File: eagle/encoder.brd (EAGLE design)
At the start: 100 x 80 mm, 11 parts, among them IC1 LM339D, U1 MCP42XXX

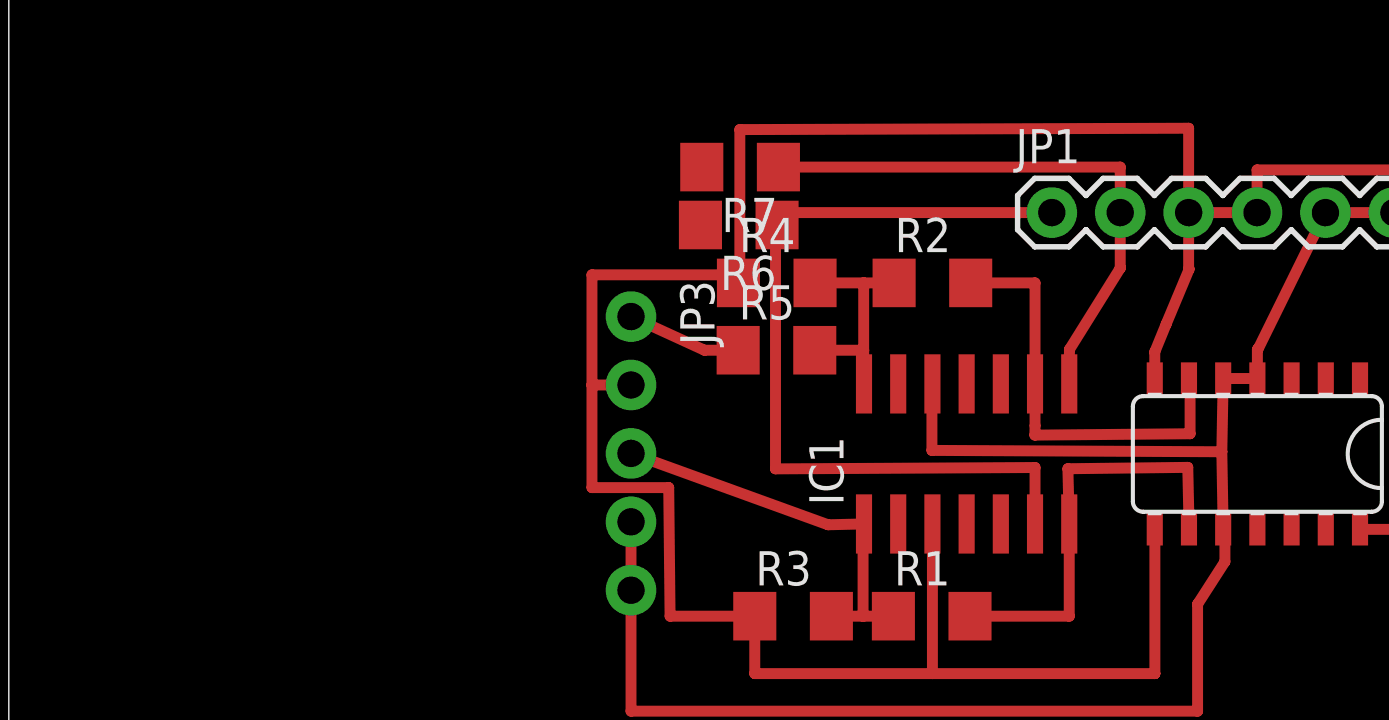
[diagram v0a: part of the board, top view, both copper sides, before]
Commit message: Added atmega.
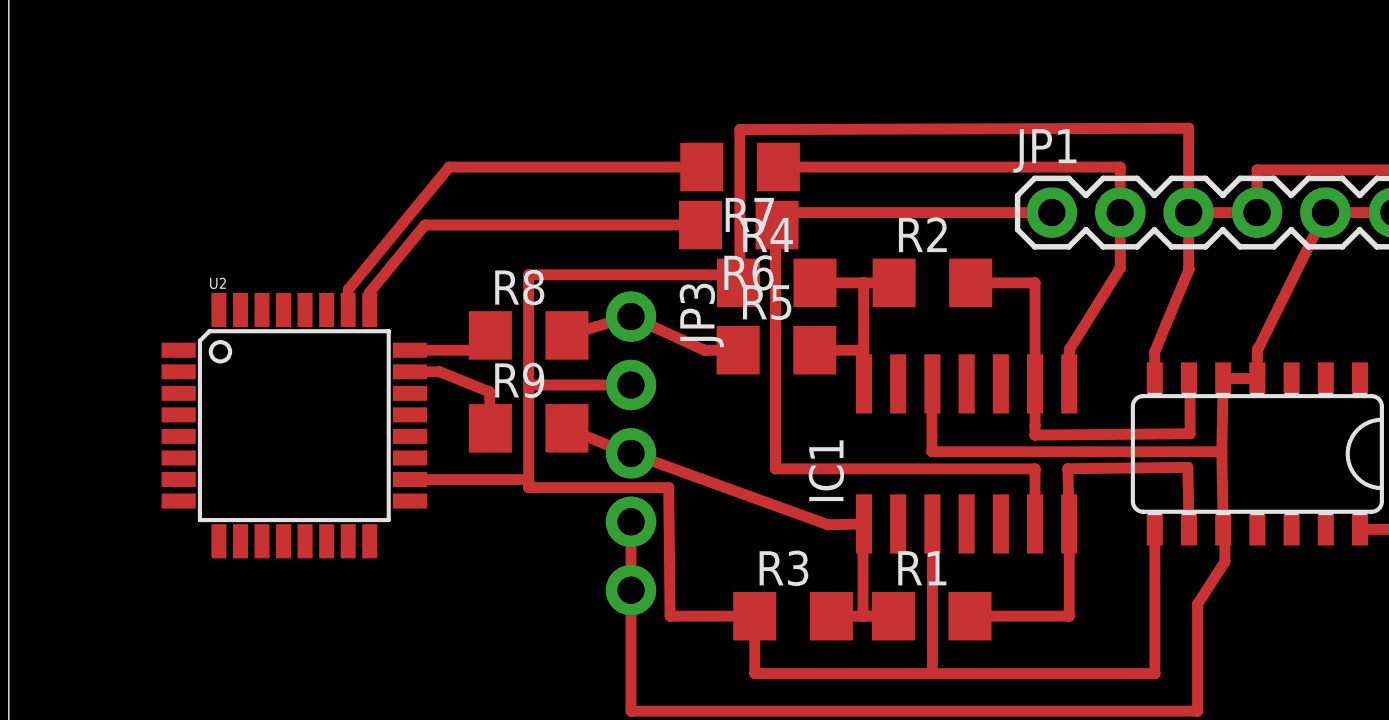
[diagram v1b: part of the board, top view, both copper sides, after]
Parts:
- added R8, R9: 0, resistor:R1206
- added U2: ATMEGA328P, SparkFun-DigitalIC:TQFP32-08
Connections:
- removed net N$2: IC1.1, JP3.3, R1.1, R3.2
- removed net N$4: JP3.1, R5.1
- new net A-ANALOG-IN: R7.2, U2.26
- new net A-DIGITAL-IN: IC1.1, JP3.3, R1.1, R3.2, R9.2
- new net B-ANALOG-IN: R6.2, U2.25
- new net B-DIGITAL-IN: JP3.1, R5.1, R8.2
- new net N$6: R8.1, U2.24
- new net N$7: R9.1, U2.23
- net +5V: now also U2.18
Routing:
- net A-DIGITAL-IN: track 0.00 -> 17.9 mm
- net A-ANALOG-IN: track 0.00 -> 16.0 mm
- net N$2: track 15.2 -> 0.00 mm
- net B-ANALOG-IN: track 0.00 -> 14.1 mm
- net +5V: track 113.3 -> 124.8 mm
- net B-DIGITAL-IN: track 0.00 -> 6.73 mm
- net N$7: track 0.00 -> 4.45 mm
- net N$4: track 4.25 -> 0.00 mm
- net N$6: track 0.00 -> 3.54 mm
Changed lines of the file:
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@@
 <element name="R6" library="resistor" package="R1206" value="0" x="27.1" y="59.3" rot="R180"/>
 <element name="R7" library="resistor" package="R1206" value="0" x="27.15" y="61.45" rot="R180"/>
+<element name="U2" library="SparkFun-DigitalIC" package="TQFP32-08" value="ATMEGA328P" x="10.6" y="51.85">
+<attribute name="PROD_ID" value="IC-09069" x="10.6" y="51.85" size="1.778" layer="27" display="off"/>
+</element>
+<element name="R8" library="resistor" package="R1206" value="0" x="19.3" y="55.2"/>
+<element name="R9" library="resistor" package="R1206" value="0" x="19.3" y="51.75"/>
 </elements>
 <signals>
@@
 <contactref element="JP1" pad="6"/>
 <wire x1="34.29" y1="53.4" x2="34.271946875" y2="53.4" width="0.4064" layer="1"/>
-<wire x1="34.271946875" y1="53.4" x2="34.271946875" y2="50.930871875" width="0.4064" layer="1"/>
-<wire x1="34.271946875" y1="50.930871875" x2="45.035" y2="50.880871875" width="0.4064" layer="1"/>
+<wire x1="34.271946875" y1="53.4" x2="34.271946875" y2="50.880871875" width="0.4064" layer="1"/>
+<wire x1="34.271946875" y1="50.880871875" x2="45.035" y2="50.880871875" width="0.4064" layer="1"/>
 <wire x1="45.035" y1="50.880871875" x2="45.085" y2="53.6" width="0.4064" layer="1"/>
 <wire x1="48.8828875" y1="59.7605125" x2="51.4228875" y2="59.7605125" width="0.4064" layer="1"/>
@@
 <wire x1="23.1" y1="41.25" x2="44.135" y2="41.25" width="0.4064" layer="1"/>
 <wire x1="44.135" y1="41.25" x2="44.135" y2="45.222" width="0.4064" layer="1"/>
-</signal>
-<signal name="N$2">
-<contactref element="R1" pad="1"/>
-<contactref element="R3" pad="2"/>
-<contactref element="IC1" pad="1"/>
-<wire x1="30.53881875" y1="44.776359375" x2="31.715234375" y2="44.776359375" width="0.4064" layer="1"/>
-<wire x1="31.715234375" y1="44.776359375" x2="32.99903125" y2="44.776359375" width="0.4064" layer="1"/>
-<wire x1="32.99903125" y1="44.776359375" x2="32.841440625" y2="44.77635625" width="0.4064" layer="1"/>
-<wire x1="31.75" y1="48.2" x2="31.715234375" y2="48.2" width="0.4064" layer="1"/>
-<contactref element="JP3" pad="3"/>
-<wire x1="31.715234375" y1="48.2" x2="31.715234375" y2="44.776359375" width="0.4064" layer="1"/>
-<wire x1="23.1" y1="50.82" x2="30.415234375" y2="48.17" width="0.4064" layer="1"/>
-<wire x1="30.415234375" y1="48.17" x2="31.715234375" y2="48.2" width="0.4064" layer="1"/>
 </signal>
 <signal name="N$5">
@@
 <wire x1="50.165" y1="48" x2="53.178775" y2="48" width="0.4064" layer="1"/>
 <contactref element="JP3" pad="2"/>
-<wire x1="23.1" y1="53.36" x2="21.65" y2="53.36" width="0.4064" layer="1"/>
-<wire x1="21.65" y1="53.36" x2="21.65" y2="57.45" width="0.4064" layer="1"/>
-<wire x1="21.65" y1="57.45" x2="27.088" y2="57.45" width="0.4064" layer="1"/>
+<wire x1="23.1" y1="53.36" x2="19.3" y2="53.36" width="0.4064" layer="1"/>
+<wire x1="19.3" y1="53.36" x2="19.3" y2="57.45" width="0.4064" layer="1"/>
+<wire x1="19.3" y1="57.45" x2="27.088" y2="57.45" width="0.4064" layer="1"/>
 <wire x1="27.088" y1="57.45" x2="27.088" y2="57.15" width="0.4064" layer="1"/>
 <wire x1="27.69481875" y1="44.776359375" x2="24.55" y2="44.776359375" width="0.4064" layer="1"/>
 <wire x1="24.55" y1="44.776359375" x2="24.5" y2="49.55" width="0.4064" layer="1"/>
-<wire x1="24.5" y1="49.55" x2="21.65" y2="49.55" width="0.4064" layer="1"/>
-<wire x1="21.65" y1="49.55" x2="21.65" y2="53.36" width="0.4064" layer="1"/>
+<wire x1="24.5" y1="49.55" x2="19.3" y2="49.55" width="0.4064" layer="1"/>
+<wire x1="19.3" y1="49.55" x2="19.3" y2="49.8" width="0.4064" layer="1"/>
+<wire x1="19.3" y1="49.85" x2="19.3" y2="53.36" width="0.4064" layer="1"/>
 <wire x1="27.69481875" y1="42.644434375" x2="27.69481875" y2="44.776359375" width="0.4064" layer="1"/>
+<contactref element="U2" pad="18"/>
+<wire x1="14.8926" y1="49.85" x2="19.3" y2="49.85" width="0.4064" layer="1"/>
+<wire x1="19.3" y1="49.85" x2="19.3" y2="49.8" width="0.4064" layer="1"/>
 </signal>
 <signal name="B-REF">
@@
 <contactref element="IC1" pad="6"/>
 <wire x1="28.46388125" y1="59.3105125" x2="28.46388125" y2="50.24568125" width="0.4064" layer="1"/>
-<wire x1="28.46388125" y1="50.24568125" x2="38.1" y2="50.29568125" width="0.4064" layer="1"/>
-<wire x1="38.1" y1="50.29568125" x2="38.1" y2="48.2" width="0.4064" layer="1"/>
+<wire x1="28.46388125" y1="50.24568125" x2="38.1" y2="50.24568125" width="0.4064" layer="1"/>
+<wire x1="38.1" y1="50.24568125" x2="38.1" y2="48.2" width="0.4064" layer="1"/>
 <contactref element="R6" pad="1"/>
 <wire x1="38.7228875" y1="59.7605125" x2="28.522" y2="59.7605125" width="0.4064" layer="1"/>
@@
 <wire x1="28.46388125" y1="59.3105125" x2="28.522" y2="59.3" width="0" layer="19" extent="1-1"/>
 </signal>
-<signal name="N$4">
+<signal name="A-ANALOG-IN">
+<contactref element="U2" pad="26"/>
+<contactref element="R7" pad="2"/>
+<wire x1="25.728" y1="61.45" x2="16.35" y2="61.45" width="0.4064" layer="1"/>
+<wire x1="16.35" y1="61.45" x2="12.6" y2="56.9" width="0.4064" layer="1"/>
+<wire x1="12.6" y1="56.9" x2="12.6" y2="56.1426" width="0.4064" layer="1"/>
+</signal>
+<signal name="B-ANALOG-IN">
+<contactref element="U2" pad="25"/>
+<contactref element="R6" pad="2"/>
+<wire x1="25.678" y1="59.3" x2="15.45" y2="59.3" width="0.4064" layer="1"/>
+<wire x1="15.45" y1="59.3" x2="13.4" y2="56.8" width="0.4064" layer="1"/>
+<wire x1="13.4" y1="56.8" x2="13.4" y2="56.1426" width="0.4064" layer="1"/>
+</signal>
+<signal name="N$6">
+<contactref element="U2" pad="24"/>
+<contactref element="R8" pad="1"/>
+<wire x1="14.8926" y1="54.65" x2="17.878" y2="54.65" width="0.4064" layer="1"/>
+<wire x1="17.878" y1="54.65" x2="17.878" y2="55.2" width="0.4064" layer="1"/>
+</signal>
+<signal name="N$7">
+<contactref element="U2" pad="23"/>
+<contactref element="R9" pad="1"/>
+<wire x1="17.878" y1="51.75" x2="17.85" y2="53.1" width="0.4064" layer="1"/>
+<wire x1="17.85" y1="53.1" x2="16" y2="53.85" width="0.4064" layer="1"/>
+<wire x1="16" y1="53.85" x2="14.8926" y2="53.85" width="0.4064" layer="1"/>
+</signal>
+<signal name="A-DIGITAL-IN">
+<contactref element="R9" pad="2"/>
+<contactref element="R1" pad="1"/>
+<contactref element="R3" pad="2"/>
+<contactref element="IC1" pad="1"/>
+<wire x1="30.53881875" y1="44.776359375" x2="31.715234375" y2="44.776359375" width="0.4064" layer="1"/>
+<wire x1="31.715234375" y1="44.776359375" x2="32.99903125" y2="44.776359375" width="0.4064" layer="1"/>
+<wire x1="32.99903125" y1="44.776359375" x2="32.841440625" y2="44.77635625" width="0.4064" layer="1"/>
+<wire x1="31.75" y1="48.2" x2="31.715234375" y2="48.2" width="0.4064" layer="1"/>
+<contactref element="JP3" pad="3"/>
+<wire x1="31.715234375" y1="48.2" x2="31.715234375" y2="44.776359375" width="0.4064" layer="1"/>
+<wire x1="23.1" y1="50.82" x2="30.415234375" y2="48.17" width="0.4064" layer="1"/>
+<wire x1="30.415234375" y1="48.17" x2="31.715234375" y2="48.2" width="0.4064" layer="1"/>
+<wire x1="20.722" y1="51.75" x2="23.15" y2="50.75" width="0.4064" layer="1"/>
+<wire x1="23.15" y1="50.75" x2="23.1" y2="50.82" width="0.4064" layer="1"/>
+</signal>
+<signal name="B-DIGITAL-IN">
+<contactref element="R8" pad="2"/>
 <contactref element="JP3" pad="1"/>
 <contactref element="R5" pad="1"/>
 <wire x1="23.1" y1="55.9" x2="25.828" y2="54.65" width="0.4064" layer="1"/>
 <wire x1="25.828" y1="54.65" x2="27.078" y2="54.65" width="0.4064" layer="1"/>
+<wire x1="20.722" y1="55.2" x2="23.05" y2="55.9" width="0.4064" layer="1"/>
+<wire x1="23.05" y1="55.9" x2="23.1" y2="55.9" width="0.4064" layer="1"/>
 </signal>
 </signals>

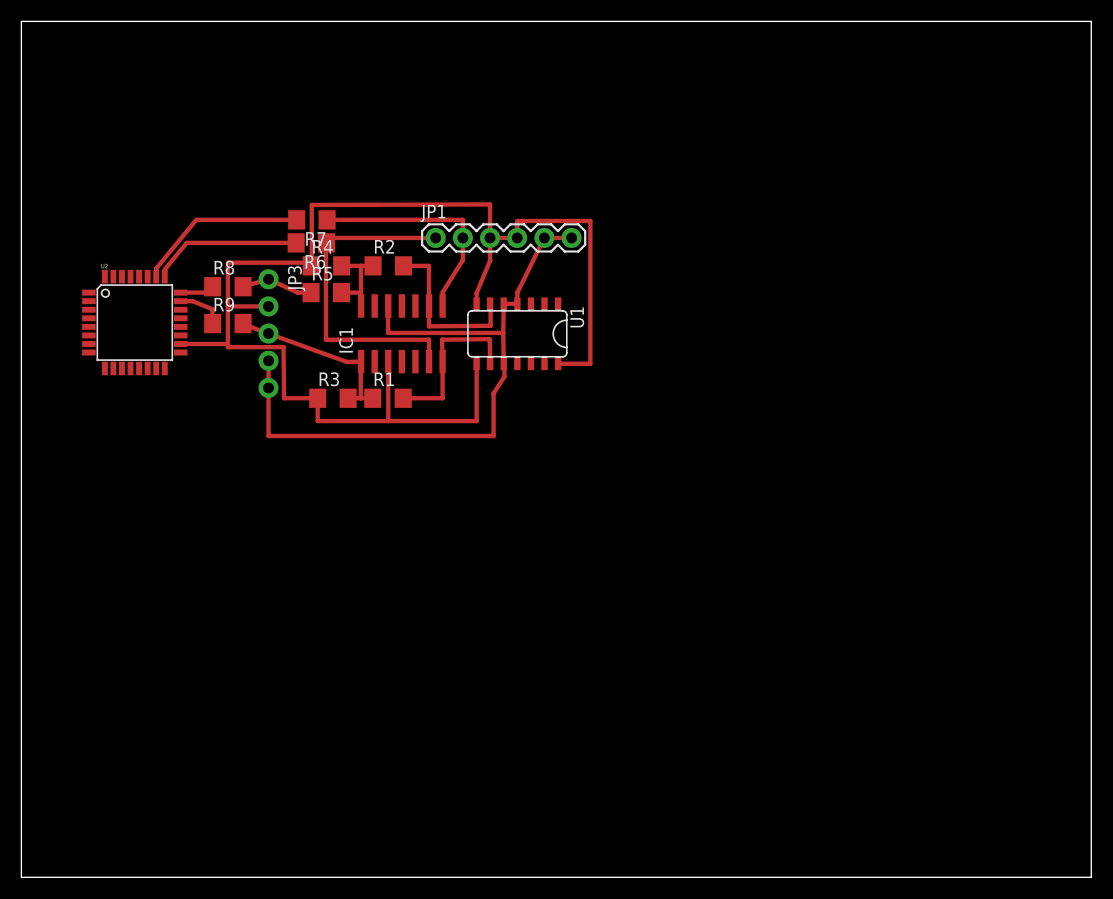
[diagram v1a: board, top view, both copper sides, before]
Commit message: Added SPI hookup
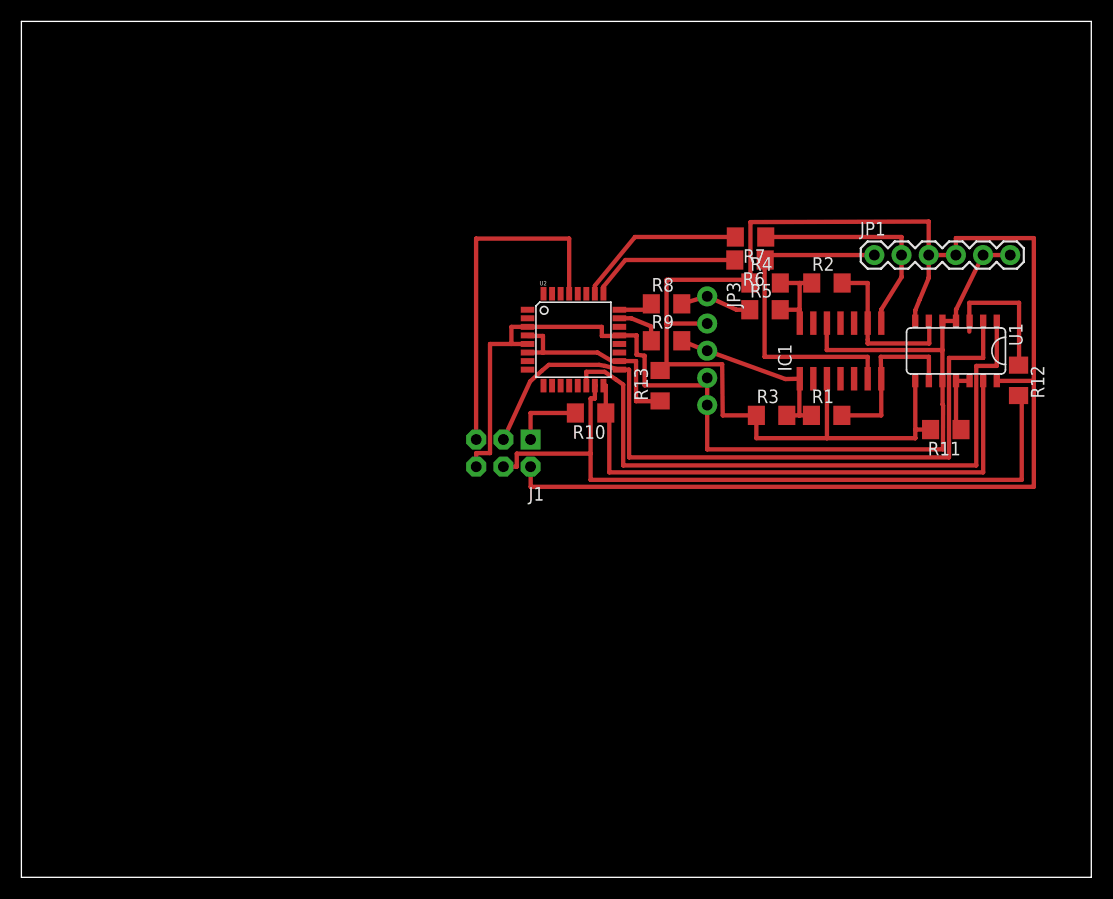
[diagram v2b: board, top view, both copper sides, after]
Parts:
- added J1: SPI, SparkFun-Connectors:2X3-NS
- added R10, R11, R12, R13: 0, resistor:R1206
- moved R2 41.0 mm to (75.3, 55.5)
- moved R7 41.0 mm to (68.2, 59.9)
- moved IC1 41.0 mm to (76.6, 49.2)
- moved JP1 41.0 mm to (79.7, 58.2)
- moved R1 41.0 mm to (75.3, 43.2)
- moved R4 41.0 mm to (69.5, 55.5)
- moved R5 41.0 mm to (69.5, 53.0)
- moved R8 41.0 mm to (60.3, 53.6)
- moved R9 41.0 mm to (60.3, 50.1)
- moved U2 41.0 mm to (51.6, 50.2)
- moved JP3 41.0 mm to (64.1, 54.3)
- moved R3 41.0 mm to (70.1, 43.2)
- moved R6 41.0 mm to (68.1, 57.7)
- moved U1 41.0 mm to (88.0, 49.2)
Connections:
- new net MISO: R10.1, U1.13, U2.16
- new net MOSI: J1.4, R12.2, U2.15
- new net N$2: J1.1, R10.2
- new net N$4: R11.1, U1.11, U1.12
- new net N$8: R12.1, U1.3
- new net N$9: R13.1, U2.18, U2.4, U2.6
- new net RESET: J1.5, U2.29
- new net SCK: J1.3, U1.2, U2.17
- new net SS: U1.1, U2.14
- net +5V: now also J1.2, R11.2, R13.2; no longer U2.18
- net GND: now also J1.6, U2.21, U2.3, U2.5
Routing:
- net SCK: track 0.00 -> 69.9 mm
- net MOSI: track 0.00 -> 67.2 mm
- net SS: track 0.00 -> 61.1 mm
- net +5V: track 124.8 -> 182.7 mm
- net MISO: track 0.00 -> 52.2 mm
- net GND: track 64.7 -> 106.3 mm
- net RESET: track 0.00 -> 32.6 mm
- net N$9: track 0.00 -> 18.7 mm
- net N$8: track 0.00 -> 13.2 mm
- net N$2: track 0.00 -> 6.67 mm
- net N$4: track 0.00 -> 6.29 mm
